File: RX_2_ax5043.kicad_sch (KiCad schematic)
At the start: 18 parts, among them U301 RFShield_OnePiece, U305 AX5043, U307 TPS22919D

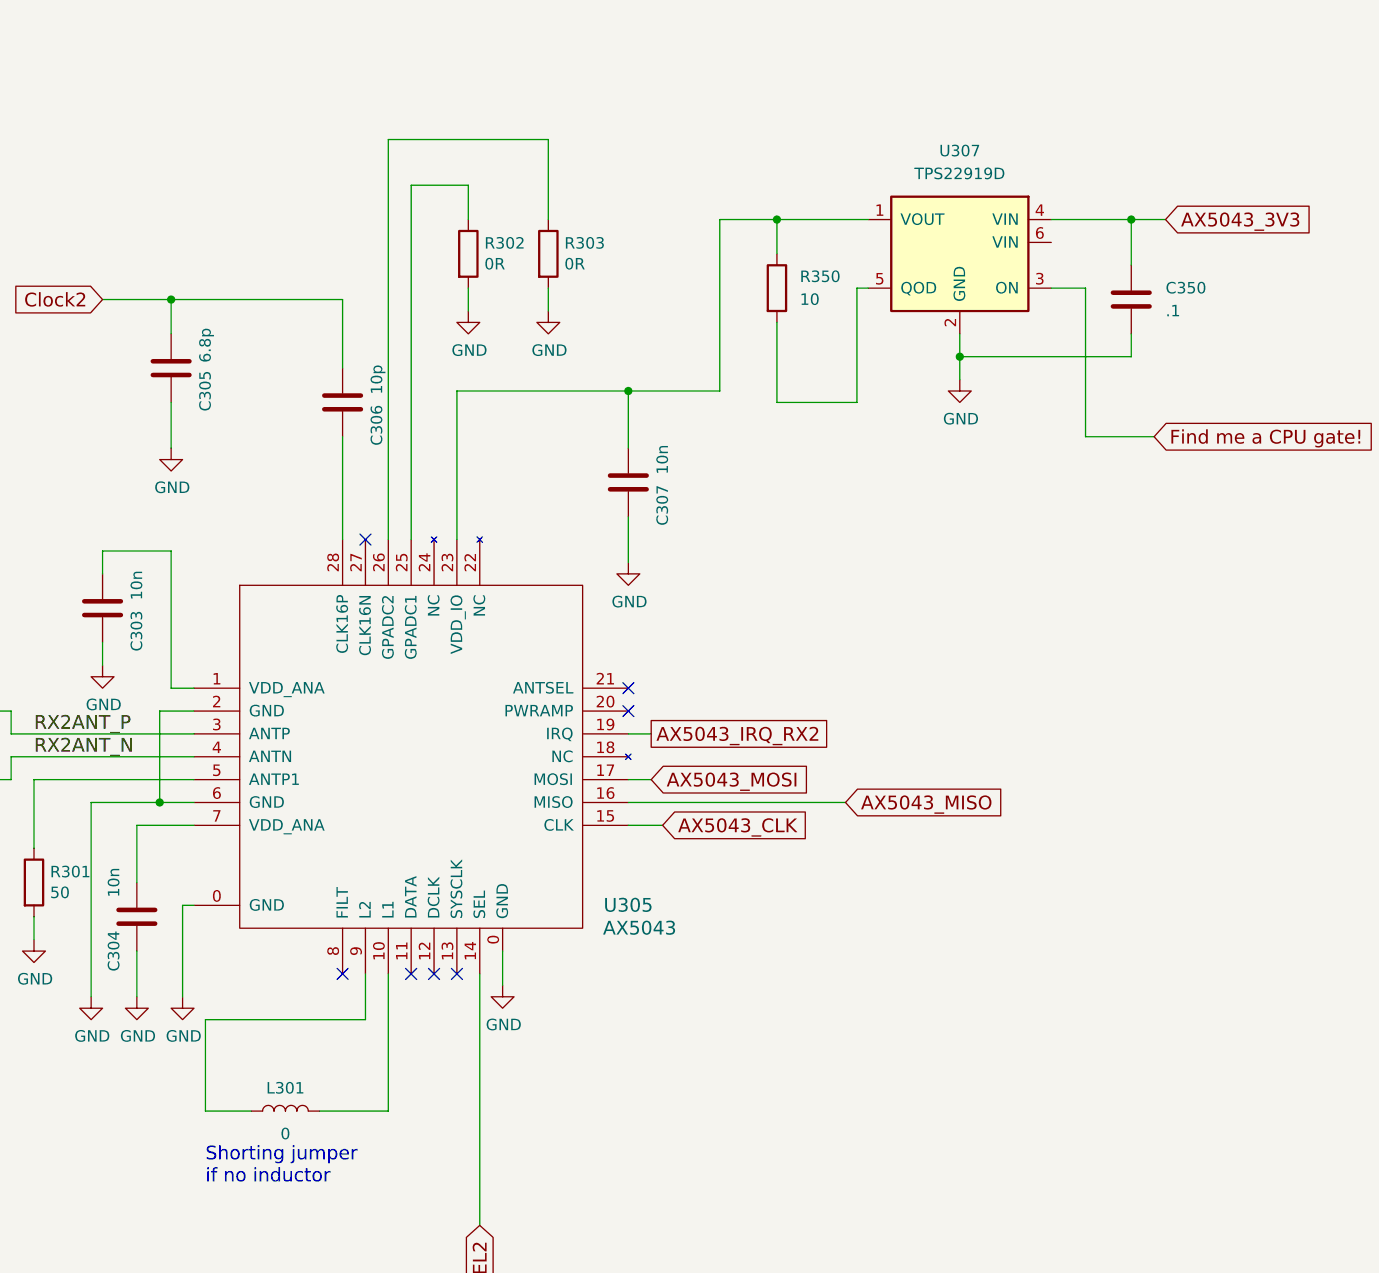
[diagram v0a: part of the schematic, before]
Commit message: Lots of cleanups to fix numerous issues
Signed-off-by: Corey Minyard <corey@minyard.net>
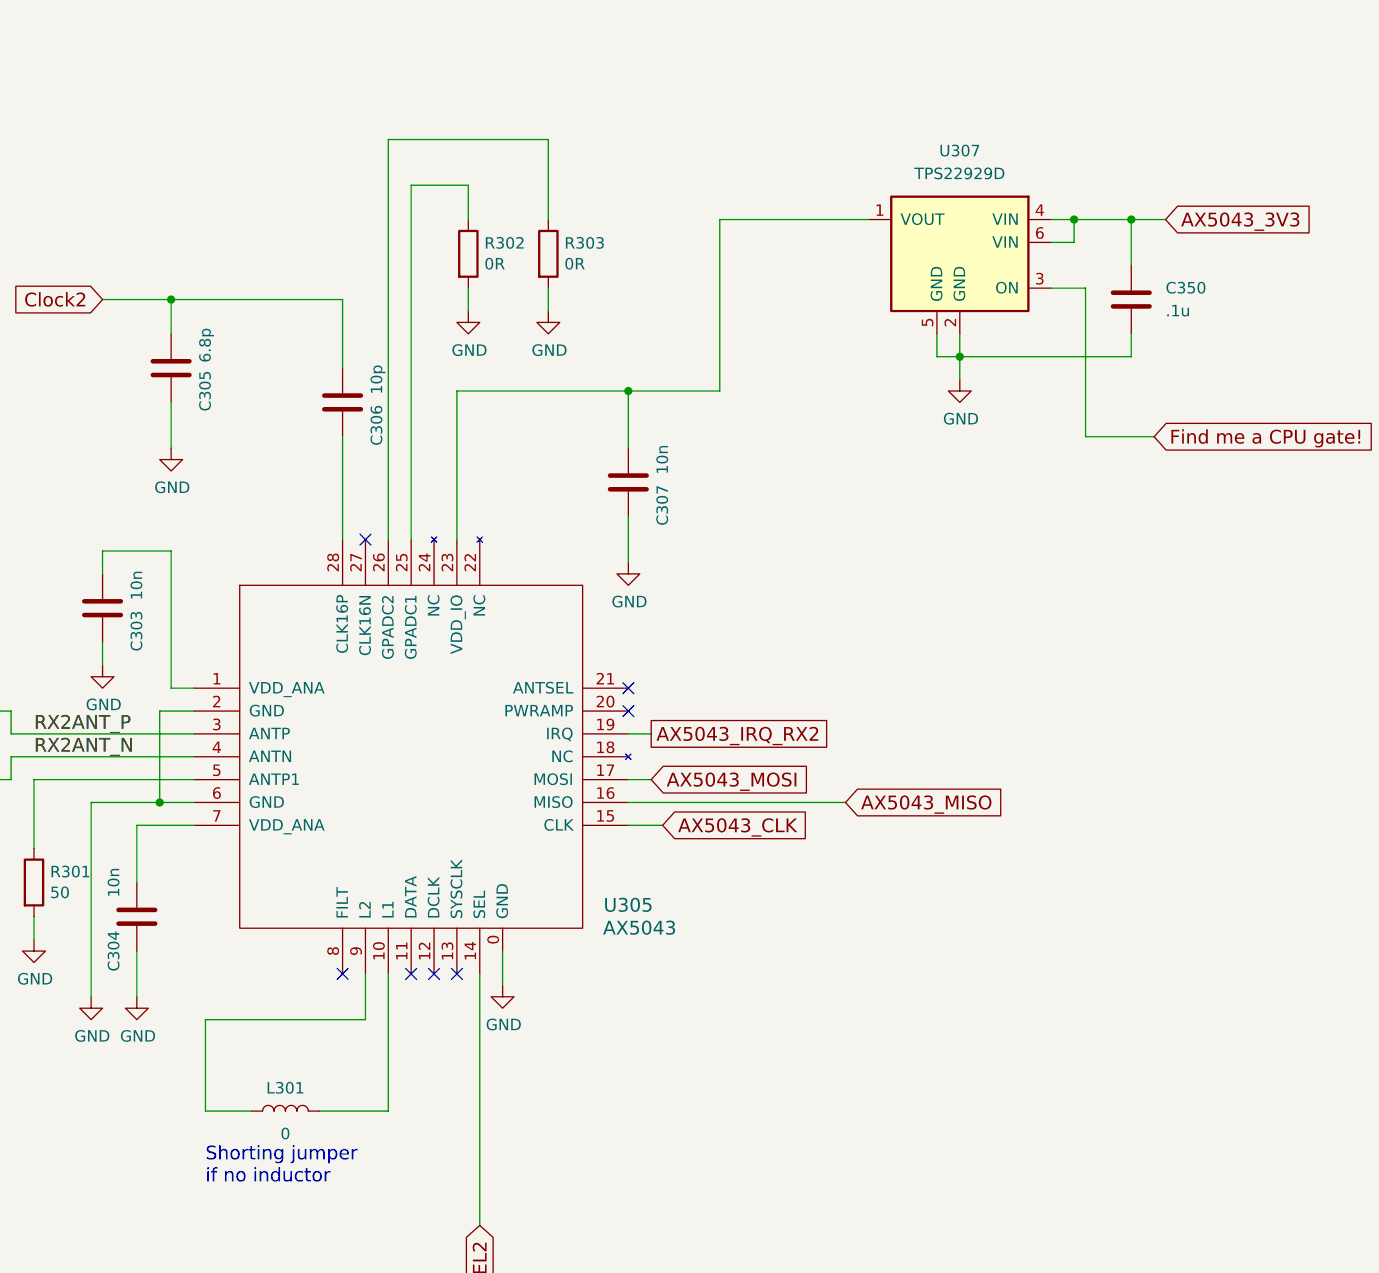
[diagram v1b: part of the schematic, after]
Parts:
- removed R350: 10, symbol Device:R
- C350: value .1 -> .1u; footprint (none) -> Capacitor_SMD:C_0402_1005Metric
- U307: value TPS22919D -> TPS22929D
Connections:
- net AX5043_3V3: now also U307.6 (VIN)
- net GND: now also U307.5 (GND)

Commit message: Start ripping things apart
Signed-off-by: Corey Minyard <corey@minyard.net>
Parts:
- removed C301, C302: 4p3, Capacitor_SMD:C_0603_1608Metric_Pad1.08x0.95mm_HandSolder, symbol Device:C
- removed P302: ~, PacSatDev_misc:U_FL, symbol PACSAT_DEV_misc:U_FL
- added L91: WBC1-1TL, IND6_WBC1, symbol PACSAT_DEV_misc:WBC1-1TL
- added R92: 10K, Resistor_SMD:R_0603_1608Metric_Pad0.98x0.95mm_HandSolder, symbol Device:R
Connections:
- net GND: now also L91.2, L91.4, R92.2
- net RX2ANT_N: now also L91.3
- net RX2ANT_P: now also L91.1
- net Find me a CPU gate! renamed AX5043_EN_RX2
- net AX5043_EN_RX2: now also R92.1
- net RX2a_P: no longer names the net of P301.1 (In)
- net RX2a_P: now also L91.6
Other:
- note removed: "All lines must be matched in length"
- note removed: "Rx2-"
- moved on the sheet: P301

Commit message: More hacking on things
Signed-off-by: Corey Minyard <corey@minyard.net>
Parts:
- removed U301: RFShield_OnePiece, PacSatDev_misc:RF_SHIELD_BMI_S_201_F_U301, symbol PACSAT_DEV_misc:RF_SHIELD_BOX

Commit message: Clean up RTC, start working on power
Signed-off-by: Corey Minyard <corey@minyard.net>
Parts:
- L91: footprint IND6_WBC1 -> PacSatDev_misc:IND6_WBC1
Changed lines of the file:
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@@
 			)
 		)
-		(property "Footprint" "IND6_WBC1"
+		(property "Footprint" "PacSatDev_misc:IND6_WBC1"
 			(at 166.37 123.19 0)
 			(effects

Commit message: Finish up most of the ax5043 routing
Signed-off-by: Corey Minyard <corey@minyard.net>
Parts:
- L301: footprint PacSatDev_misc:L_Murata_LQH2MCNxxxx02_2.0x1.6mm -> Inductor_SMD:L_0603_1608Metric_Pad1.05x0.95mm_HandSolder
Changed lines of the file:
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@@
 			)
 		)
-		(property "Footprint" "PacSatDev_misc:L_Murata_LQH2MCNxxxx02_2.0x1.6mm"
+		(property "Footprint" "Inductor_SMD:L_0603_1608Metric_Pad1.05x0.95mm_HandSolder"
 			(at 204.47 168.91 0)
 			(effects

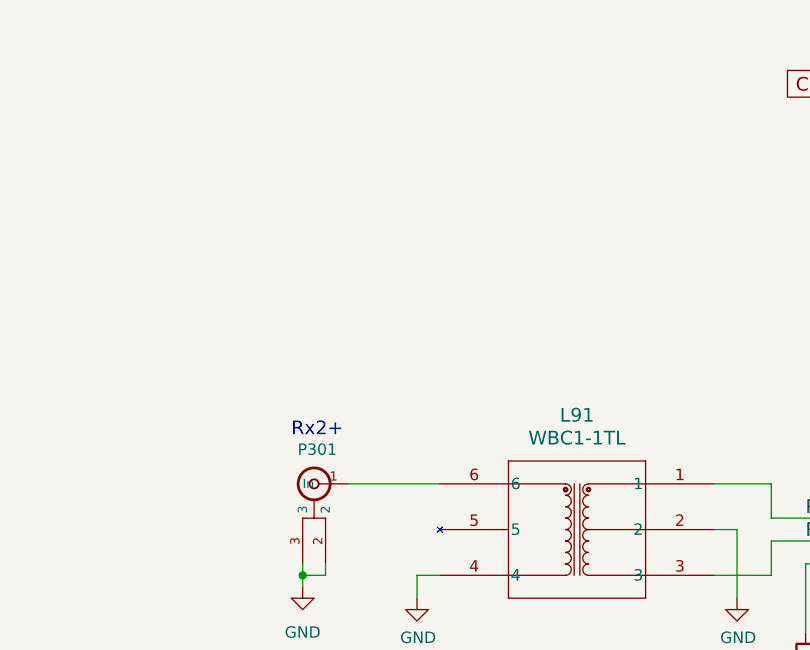
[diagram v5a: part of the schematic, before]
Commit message: Do a lot of routing work
RX input is done, 5043s are done, power is done.

Signed-off-by: Corey Minyard <corey@minyard.net>
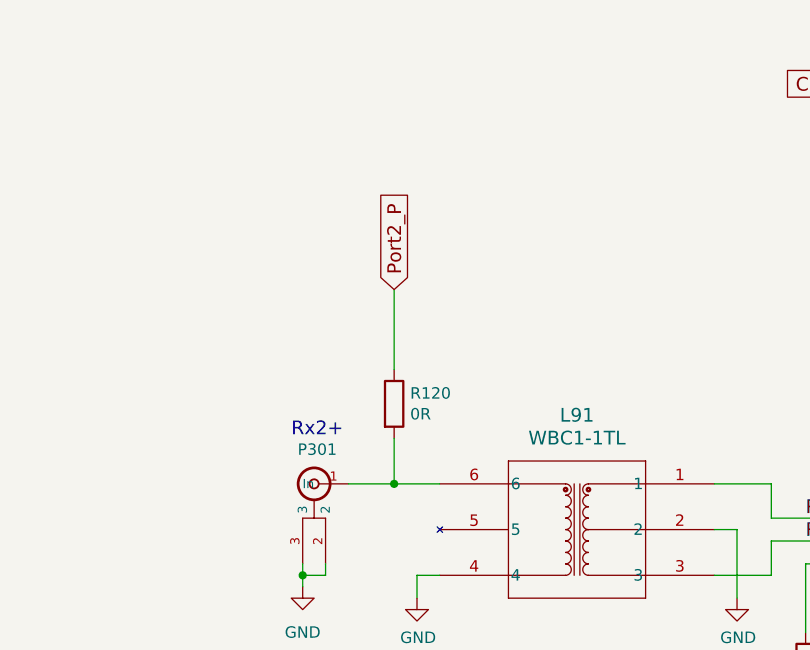
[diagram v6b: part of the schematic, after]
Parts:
- added R120: 0R, Resistor_SMD:R_0603_1608Metric_Pad0.98x0.95mm_HandSolder, symbol Device:R
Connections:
- net at L91.6, P301.1 (In): now also R120.2
- new net Port2_P: R120.1
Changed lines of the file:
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@@
+	)
+	(junction
+		(at 130.81 123.19)
+		(diameter 0)
+		(color 0 0 0 0)
 	)
 	(junction
@@
 	(wire
 		(pts
+			(xy 130.81 118.11) (xy 130.81 123.19)
+		)
+		(stroke
+			(width 0)
+			(type default)
+		)
+	)
+	(wire
+		(pts
 			(xy 191.77 121.92) (xy 191.77 106.68)
 		)
@@
 	(wire
 		(pts
+			(xy 130.81 101.6) (xy 130.81 110.49)
+		)
+		(stroke
+			(width 0)
+			(type default)
+		)
+	)
+	(wire
+		(pts
+			(xy 130.81 123.19) (xy 135.89 123.19)
+		)
+		(stroke
+			(width 0)
+			(type default)
+		)
+	)
+	(wire
+		(pts
 			(xy 123.19 132.08) (xy 123.19 133.35)
 		)
@@
 	(wire
 		(pts
-			(xy 125.73 123.19) (xy 135.89 123.19)
+			(xy 125.73 123.19) (xy 130.81 123.19)
 		)
 		(stroke
@@
 				)
 				(justify right)
+				(hide yes)
+			)
+		)
+	)
+	(global_label "Port2_P"
+		(shape input)
+		(at 130.81 101.6 90)
+		(fields_autoplaced yes)
+		(effects
+			(font
+				(size 1.524 1.524)
+			)
+			(justify left)
+		)
+		(property "Intersheetrefs" "${INTERSHEET_REFS}"
+			(at 130.81 89.9495 90)
+			(effects
+				(font
+					(size 1.27 1.27)
+				)
+				(justify left)
 				(hide yes)
 			)
@@
 					(unit 1)
 				)
+			)
+		)
+	)
+	(symbol
+		(lib_id "Device:R")
+		(at 130.81 114.3 0)
+		(unit 1)
+		(exclude_from_sim no)
+		(in_bom yes)
+		(on_board yes)
+		(dnp no)
+		(property "Reference" "R120"
+			(at 132.588 113.1316 0)
+			(effects
+				(font
+					(size 1.27 1.27)
+				)
+				(justify left)
+			)
+		)
+		(property "Value" "0R"
+			(at 132.588 115.443 0)
+			(effects
+				(font
+					(size 1.27 1.27)
+				)
+				(justify left)
+			)
+		)
+		(property "Footprint" "Resistor_SMD:R_0603_1608Metric_Pad0.98x0.95mm_HandSolder"
+			(at 129.032 114.3 90)
+			(effects
+				(font
+					(size 1.27 1.27)
+				)
+				(hide yes)
+			)
+		)
+		(property "Datasheet" "~"
+			(at 130.81 114.3 0)
+			(effects
+				(font
+					(size 1.27 1.27)
+				)
+			)
+		)
+		(property "Description" ""
+			(at 130.81 114.3 0)
+			(effects
+				(font
+					(size 1.27 1.27)
+				)
+			)
+		)
+		(pin "1"
+		)
+		(pin "2"
+		)
+		(instances
+			(project "PacSat_AFSK"
+				(path "/cc9f42d2-6985-41ac-acab-5ab7b01c5b38/1e7123c2-80dc-43cd-b90a-12f3fe1af0cb"
+					(reference "R120")
+					(unit 1)
+				)

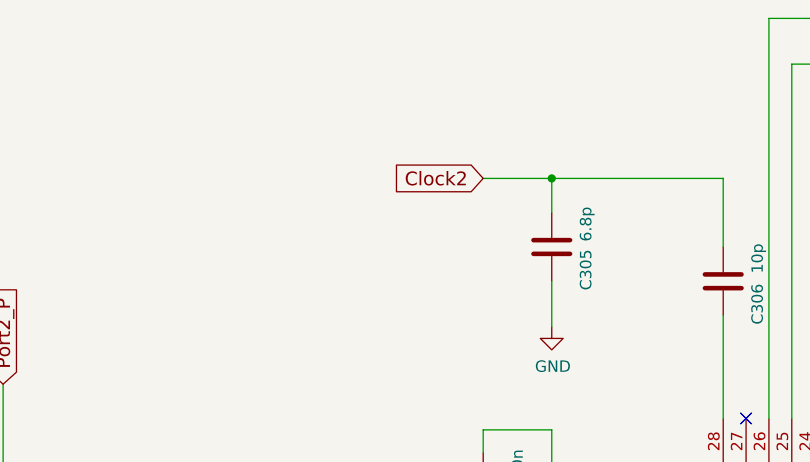
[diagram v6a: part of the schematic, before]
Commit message: Wire in clocks, more cleanups, wire in MRAM
Signed-off-by: Corey Minyard <corey@minyard.net>
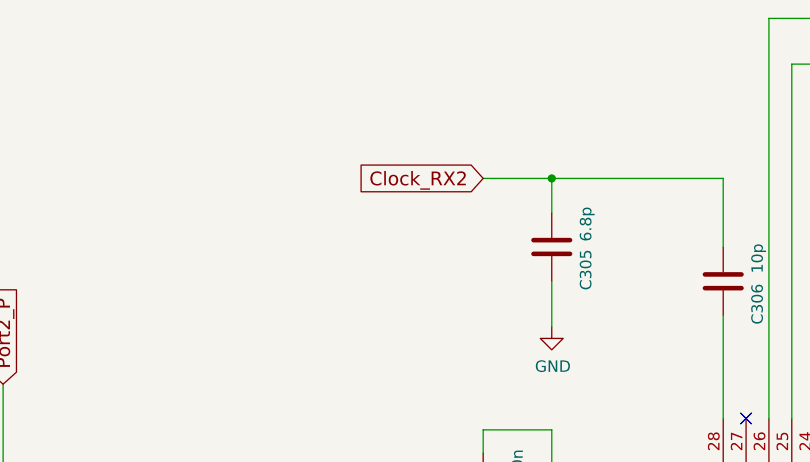
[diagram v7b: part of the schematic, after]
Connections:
- net Clock2 renamed Clock_RX2
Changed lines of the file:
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@@
 		)
 	)
-	(global_label "Clock2"
+	(global_label "Clock_RX2"
 		(shape input)
 		(at 184.15 78.74 180)
@@
 		)
 		(property "Intersheetrefs" "${INTERSHEET_REFS}"
-			(at 173.756 78.74 0)
+			(at 169.5241 78.74 0)
 			(effects
 				(font

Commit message: Finish up and clean up a lot of things
Signed-off-by: Corey Minyard <corey@minyard.net>
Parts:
- added R128: 1K, Resistor_SMD:R_0603_1608Metric_Pad0.98x0.95mm_HandSolder, symbol Device:R
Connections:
- net AX5043_CLK: now also R128.2; no longer U305.15 (CLK)
- new net: R128.1, U305.15 (CLK)
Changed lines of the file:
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@@
+	(wire
+		(pts
+			(xy 259.08 137.16) (xy 266.7 137.16)
+		)
+		(stroke
+			(width 0)
+			(type default)
+		)
+	)
 	(wire
 		(pts
@@
 	(wire
 		(pts
-			(xy 242.57 137.16) (xy 246.38 137.16)
+			(xy 242.57 137.16) (xy 251.46 137.16)
 		)
 		(stroke
@@
 	(global_label "AX5043_CLK"
 		(shape input)
-		(at 246.38 137.16 0)
+		(at 266.7 137.16 0)
 		(fields_autoplaced yes)
 		(effects
@@
 		)
 		(property "Intersheetrefs" "${INTERSHEET_REFS}"
-			(at 263.0875 137.16 0)
+			(at 283.4075 137.16 0)
 			(effects
 				(font
@@
 					(unit 1)
 				)
+			)
+		)
+	)
+	(symbol
+		(lib_id "Device:R")
+		(at 255.27 137.16 90)
+		(unit 1)
+		(exclude_from_sim no)
+		(in_bom yes)
+		(on_board yes)
+		(dnp no)
+		(property "Reference" "R128"
+			(at 255.524 139.446 90)
+			(effects
+				(font
+					(size 1.27 1.27)
+				)
+			)
+		)
+		(property "Value" "1K"
+			(at 255.524 141.986 90)
+			(effects
+				(font
+					(size 1.27 1.27)
+				)
+			)
+		)
+		(property "Footprint" "Resistor_SMD:R_0603_1608Metric_Pad0.98x0.95mm_HandSolder"
+			(at 255.27 138.938 90)
+			(effects
+				(font
+					(size 1.27 1.27)
+				)
+				(hide yes)
+			)
+		)
+		(property "Datasheet" "~"
+			(at 255.27 137.16 0)
+			(effects
+				(font
+					(size 1.27 1.27)
+				)
+				(hide yes)
+			)
+		)
+		(property "Description" "Resistor"
+			(at 255.27 137.16 0)
+			(effects
+				(font
+					(size 1.27 1.27)
+				)
+				(hide yes)
+			)
+		)
+		(pin "1"
+		)
+		(pin "2"
+		)
+		(instances
+			(project "PacSat_AFSK"
+				(path "/cc9f42d2-6985-41ac-acab-5ab7b01c5b38/1e7123c2-80dc-43cd-b90a-12f3fe1af0cb"
+					(reference "R128")
+					(unit 1)
+				)
